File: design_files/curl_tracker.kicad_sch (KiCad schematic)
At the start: 38 parts, among them J1 JST-PH, J2 USB_C_Receptacle, J3 SSD1306 OLED, J4 JST-PH, Q1 DMP2035, Q2 AO3400A, SW1 SW_Push, SW2 SW_Push, SW3 SW_Push, U1 AP2112K-3.3, U2 ESP32-C3-MINI-1, U3 MCP73831-2-OT, U4 BMI270, U5 USBLC6-2SC6

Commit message: image fix
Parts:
- C1, C3, C5, C8, C9: footprint (none) -> Capacitor_SMD:C_0402_1005Metric
- C2, C4: footprint (none) -> Capacitor_SMD:C_0805_2012Metric
- C6, C7: footprint (none) -> Capacitor_SMD:C_0603_1608Metric
- D1: footprint (none) -> Diode_SMD:D_SOD-123
- D2: footprint (none) -> LED_SMD:LED_0603_1608Metric
- J1, J4: footprint (none) -> Connector_JST:JST_PH_S2B-PH-K_1x02_P2.00mm_Horizontal
- J2: footprint (none) -> Connector_USB:USB_C_Receptacle_GCT_USB4115-03-C
- J3: footprint (none) -> Connector_PinSocket_2.54mm:PinSocket_1x04_P2.54mm_Vertical
- Q1: footprint (none) -> Package_TO_SOT_SMD:SOT-23
- R12: footprint (none) -> Resistor_SMD:R_0402_1005Metric
- SW1, SW2, SW3: footprint (none) -> Button_Switch_SMD:SW_SPST_TL3342

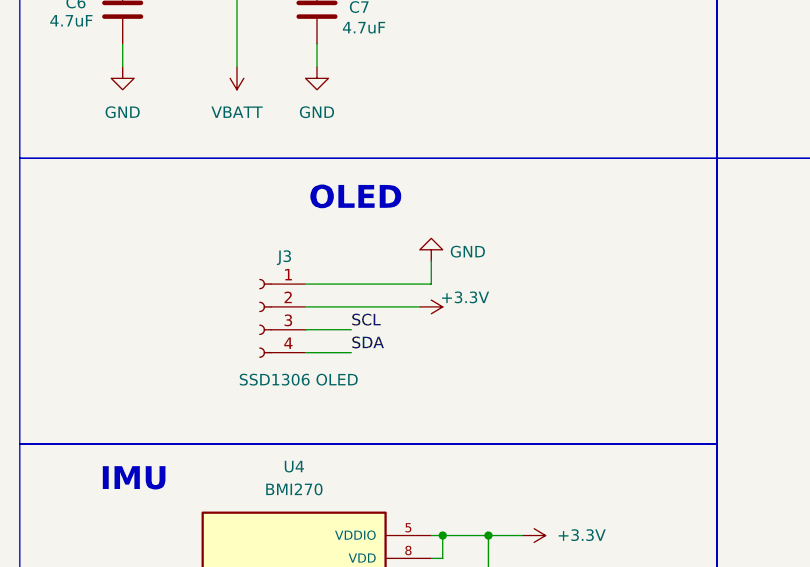
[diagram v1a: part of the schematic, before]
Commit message: start of esp-idf transition
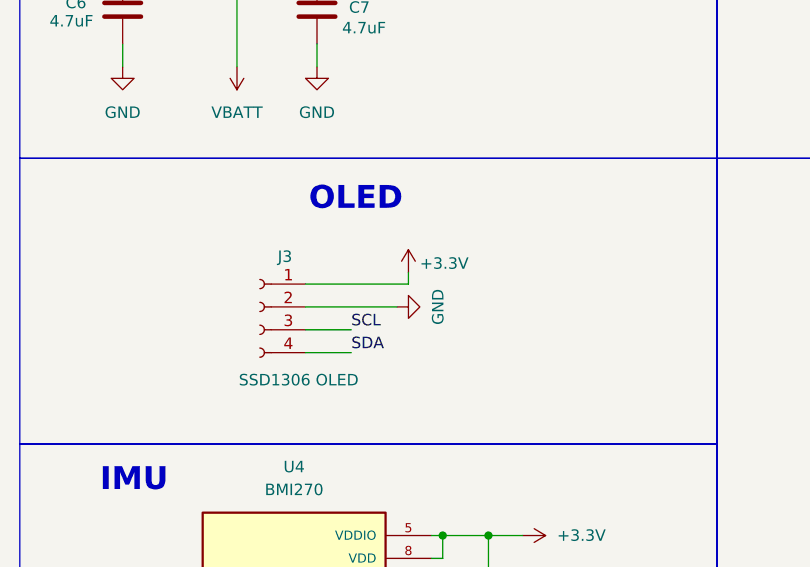
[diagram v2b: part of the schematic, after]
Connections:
- net +3.3V: now also J3.1 (Pin_1); no longer J3.2 (Pin_2)
- net GND: now also J3.2 (Pin_2); no longer J3.1 (Pin_1)
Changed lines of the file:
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@@
 	(wire
 		(pts
-			(xy 44.45 130.81) (xy 57.15 130.81)
-		)
-		(stroke
-			(width 0)
-			(type default)
-		)
-	)
-	(wire
-		(pts
 			(xy 43.18 30.48) (xy 49.53 30.48)
 		)
@@
 	(wire
 		(pts
-			(xy 58.42 128.27) (xy 44.45 128.27)
+			(xy 44.45 128.27) (xy 55.88 128.27)
 		)
 		(stroke
@@
 	(wire
 		(pts
-			(xy 58.42 125.73) (xy 58.42 128.27)
-		)
-		(stroke
-			(width 0)
-			(type default)
-		)
-	)
-	(wire
-		(pts
 			(xy 261.62 58.42) (xy 267.97 58.42)
 		)
@@
 	(wire
 		(pts
+			(xy 55.88 128.27) (xy 55.88 127)
+		)
+		(stroke
+			(width 0)
+			(type default)
+		)
+	)
+	(wire
+		(pts
 			(xy 254 44.45) (xy 261.62 44.45)
 		)
@@
 	(wire
 		(pts
+			(xy 44.45 130.81) (xy 54.61 130.81)
+		)
+		(stroke
+			(width 0)
+			(type default)
+		)
+	)
+	(wire
+		(pts
 			(xy 194.31 87.63) (xy 203.2 87.63)
 		)
@@
 	(symbol
 		(lib_id "power:GND")
-		(at 58.42 125.73 180)
+		(at 54.61 130.81 90)
 		(unit 1)
 		(body_style 1)
@@
 		(dnp no)
 		(property "Reference" "#PWR038"
-			(at 58.42 119.38 0)
+			(at 60.96 130.81 0)
 			(hide yes)
 			(show_name no)
@@
 		)
 		(property "Value" "GND"
-			(at 62.484 124.714 0)
+			(at 59.182 130.81 0)
 			(show_name no)
 			(do_not_autoplace no)
@@
 		)
 		(property "Footprint" ""
-			(at 58.42 125.73 0)
+			(at 54.61 130.81 0)
 			(hide yes)
 			(show_name no)
@@
 		)
 		(property "Datasheet" ""
-			(at 58.42 125.73 0)
+			(at 54.61 130.81 0)
 			(hide yes)
 			(show_name no)
@@
 		)
 		(property "Description" "Power symbol creates a global label with name \"GND\" , ground"
-			(at 58.42 125.73 0)
+			(at 54.61 130.81 0)
 			(hide yes)
 			(show_name no)
@@
 	(symbol
 		(lib_id "power:+3.3V")
-		(at 57.15 130.81 270)
+		(at 55.88 127 0)
 		(unit 1)
 		(body_style 1)
@@
 		(dnp no)
 		(property "Reference" "#PWR018"
-			(at 53.34 130.81 0)
+			(at 55.88 130.81 0)
 			(hide yes)
 			(show_name no)
@@
 		)
 		(property "Value" "+3.3V"
-			(at 59.436 129.794 90)
+			(at 57.15 125.984 0)
 			(show_name no)
 			(do_not_autoplace no)
@@
 		)
 		(property "Footprint" ""
-			(at 57.15 130.81 0)
+			(at 55.88 127 0)
 			(hide yes)
 			(show_name no)
@@
 		)
 		(property "Datasheet" ""
-			(at 57.15 130.81 0)
+			(at 55.88 127 0)
 			(hide yes)
 			(show_name no)
@@
 		)
 		(property "Description" "Power symbol creates a global label with name \"+3.3V\""
-			(at 57.15 130.81 0)
+			(at 55.88 127 0)
 			(hide yes)
 			(show_name no)

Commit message: finished schematic
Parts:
- removed C1, C3: 1uF, Capacitor_SMD:C_0402_1005Metric, symbol Device:C
- removed C2: 10uF, Capacitor_SMD:C_0805_2012Metric, symbol Device:C
- removed C6, C7: 4.7uF, Capacitor_SMD:C_0603_1608Metric, symbol Device:C
- removed C8, C9: 100nF, Capacitor_SMD:C_0402_1005Metric, symbol Device:C
- removed R1, R10: 100k, Resistor_SMD:R_0402_1005Metric, symbol Device:R
- removed R11: 100, Resistor_SMD:R_0402_1005Metric, symbol Device:R
- removed R12, R5, R6: 4.7k, Resistor_SMD:R_0402_1005Metric, symbol Device:R
- removed R2, R3: 5.1k, Resistor_SMD:R_0402_1005Metric, symbol Device:R
- removed R4, R9: 10k, Resistor_SMD:R_0402_1005Metric, symbol Device:R
- removed R7: 470, Resistor_SMD:R_0402_1005Metric, symbol Device:R
- removed R8: 5k, Resistor_SMD:R_0402_1005Metric, symbol Device:R
- removed U1: AP2112K-3.3, Package_TO_SOT_SMD:SOT-23-5, symbol Regulator_Linear:AP2112K-3.3
- removed U4: BMI270, BMI270:XDCR_BMI270, symbol BMI:BMI270
- added C1, C2, C3, C4: 10uF, Capacitor_SMD:C_0805_2012Metric, symbol Device:C_Small
- added C10, C11: 4.7uF, Capacitor_SMD:C_0805_2012Metric, symbol Device:C_Small
- added C12, C15, C6, C9: 100nF, Capacitor_SMD:C_0402_1005Metric, symbol Device:C_Small
- added C13, C14: 100nF, Capacitor_SMD:C_0805_2012Metric, symbol Device:C_Small
- added C5: 1uF, Capacitor_SMD:C_0805_2012Metric, symbol Device:C_Small
- added L1: 2.2uH, Inductor_SMD:L_Coilcraft_LPS4018, symbol Device:L_Small
- added R1, R4, R5: 100k, Resistor_SMD:R_0402_1005Metric, symbol Device:R_Small
- added R11, R12, R17, R19, R3, R6: 10k, Resistor_SMD:R_0402_1005Metric, symbol Device:R_Small
- added R13, R14: 5.1k, Resistor_SMD:R_0402_1005Metric, symbol Device:R_Small
- added R15: 470, Resistor_SMD:R_0402_1005Metric, symbol Device:R_Small
- added R16: 5k, Resistor_SMD:R_0402_1005Metric, symbol Device:R_Small
- added R18, R2: 100, Resistor_SMD:R_0402_1005Metric, symbol Device:R_Small
- added R7, R8: 4.7k, Resistor_SMD:R_0402_1005Metric, symbol Device:R_Small
- added U1: TPS63001, Package_SON:Texas_DRC0010J_ThermalVias, symbol Regulator_Switching:TPS63001
- added U4: BMI270, BMI270:XDCR_BMI270, symbol BMI270:BMI270
- D3: footprint Diode_THT:D_DO-41_SOD81_P10.16mm_Horizontal -> Diode_SMD:D_SOD-123
- SW1, SW2, SW3: footprint Button_Switch_SMD:SW_SPST_TL3342 -> Button_Switch_SMD:SW_SPST_TL3305A
- renumbered C4 to C7, C5 to C8
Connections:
- net +3.3V: now also J3.2 (Pin_2), C12.2, C13.1, C14.1, C15.1, C3.2, C4.2, R11.2, R12.2, R17.1, R3.1, R6.1, R7.1, R8.1, U1.1 (VOUT), U1.10 (FB), U4.12 (CSB), U4.2 (ASDX), U4.3 (ASCX), U4.5 (VDDIO), U4.8 (VDD); no longer J3.1 (Pin_1)
- net +5V: now also C10.1, C9.2, R1.1
- net GND: now also J3.1 (Pin_1), Q2.2 (S), SW2.2, C1.1, C10.2, C11.2, C12.1, C13.2, C14.2, C2.2, C3.1, C4.1, C5.2, C6.2, C9.1, R1.2, R13.2, R14.2, R16.1, R19.1, R5.2, U1.11 (PGND), U1.3 (PGND), U1.7 (PS/SYNC), U1.9 (GND), U4.1 (SDO), U4.6 (GNDIO), U4.7 (GND); no longer J3.2 (Pin_2), Q2.3 (D), SW2.1
- net SCL: now also U2.20 (GPIO6), R7.2, U4.13 (SCX); no longer SW2.2, U2.23 (GPIO9)
- net SDA: now also U2.21 (GPIO7), R8.2, U4.14 (SDX); no longer U2.22 (GPIO8)
- net USB_N: now also U5.4 (I/O2); no longer U5.6 (I/O1)
- net USB_P: now also U5.6 (I/O1); no longer U5.4 (I/O2)
- net VBATT: now also C11.1, R4.1
- net at D1.1 (K), Q1.3 (S): now also C1.2, R2.1, U1.5 (VIN)
- net at U2.5 (GPIO2/ADC1_CH2): now also R6.2
- net at Q2.1 (G): now also R18.2, R19.2
- net at U2.12 (GPIO0/ADC1_CH0/XTAL_32K_P): now also C6.1, R4.2, R5.1
- net at SW1.2, U2.8 (EN/CHIP_PU): now also C5.1, R3.2
- net at U3.1 (STAT): now also R15.1
- net at U3.5 (PROG): now also R16.2
- net at D3.2 (A), J4.2 (Pin_2): now also Q2.3 (D), C15.2; no longer Q2.2 (S)
- net at J2.A5 (CC1): now also R13.1
- net at J2.B5 (CC2): now also R14.1
- net at D2.1 (K): now also R15.2
- net GPIO4 renamed IO4
- net IO4: now also R18.1
- net GPIO5 renamed IO5
- net IO5: now also R17.2
- net INTR renamed IO3
- net IO3: now also U4.4 (INT1)
- new net: L1.1, U1.2 (L2)
- new net: L1.2, U1.4 (L1)
- new net: R11.1, U2.22 (GPIO8)
- new net: R12.1, SW2.1, U2.23 (GPIO9)
- new net: C2.1, R2.2, U1.6 (EN), U1.8 (VINA)
- no-connect marks 20 -> 17
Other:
- note added: "BOOT"
- note added: "RESET"
- moved on the sheet: C7, C8, D1, D2, D3, J1, J3, J4, Q1, Q2, SW1, SW2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

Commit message: finished schematic
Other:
- moved on the sheet: C1, C2, C3, C4, D1, J1, L1, Q1, R1, R17, R2, SW3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
